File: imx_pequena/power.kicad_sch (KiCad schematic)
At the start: 25 parts

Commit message: Updated config
Updated config file and some pins
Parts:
- gave numbers to parts that had none: 25

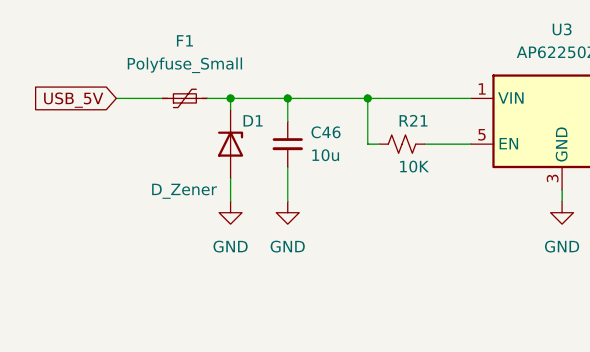
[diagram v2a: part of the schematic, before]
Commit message: Cleaned up NVCC pins
Added 3v3 connections + decoupling caps to NVcc pins
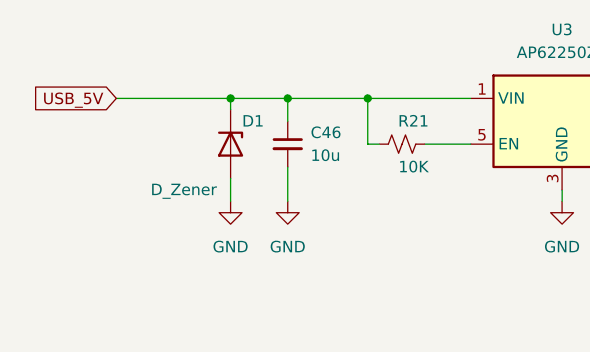
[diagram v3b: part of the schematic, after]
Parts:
- removed F1: Polyfuse_Small, symbol Device:Polyfuse_Small
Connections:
- net USB_5V: now also C46.1, D1.1 (K), R21.1, U3.1 (VIN)
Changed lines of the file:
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@@
-    (stroke (width 0) (type default) (color 0 0 0 0))
-  )
-  (wire (pts (xy 73.66 54.61) (xy 76.2 54.61))
     (stroke (width 0) (type default) (color 0 0 0 0))
   )
@@
     (stroke (width 0) (type default) (color 0 0 0 0))
   )
-  (wire (pts (xy 63.5 54.61) (xy 68.58 54.61))
+  (wire (pts (xy 63.5 54.61) (xy 76.2 54.61))
     (stroke (width 0) (type default) (color 0 0 0 0))
   )
@@
       (effects (font (size 1.27 1.27)) hide)
     )
-    (pin "1")
-    (pin "2")
-  )
-  (symbol (lib_id "Device:Polyfuse_Small") (at 71.12 54.61 90) (unit 1)
-    (in_bom yes) (on_board yes) (fields_autoplaced)
-    (property "Reference" "F1" (id 0) (at 71.12 48.26 90))
-    (property "Value" "Polyfuse_Small" (id 1) (at 71.12 50.8 90))
-    (property "Footprint" "" (id 2) (at 76.2 53.34 0)
-      (effects (font (size 1.27 1.27)) (justify left) hide)
-    )
-    (property "Datasheet" "~" (id 3) (at 71.12 54.61 0)
-      (effects (font (size 1.27 1.27)) hide)
-    )

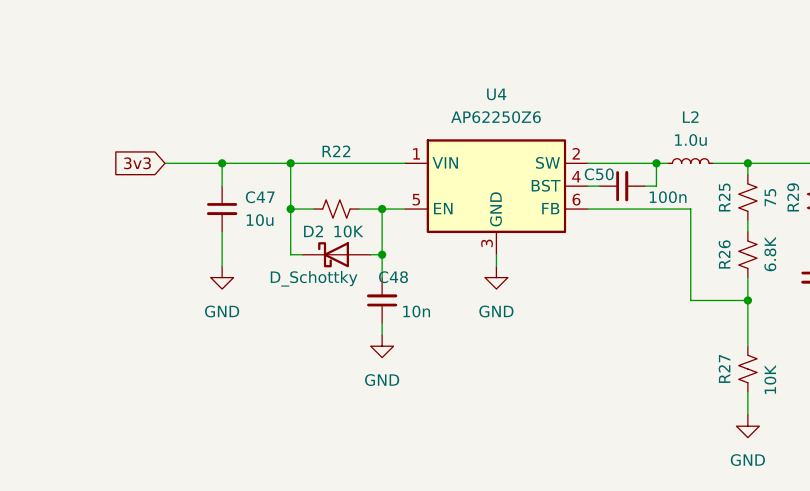
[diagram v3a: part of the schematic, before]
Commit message: Part Assignment
Assigned GPIOs and assigned footprints to most parts
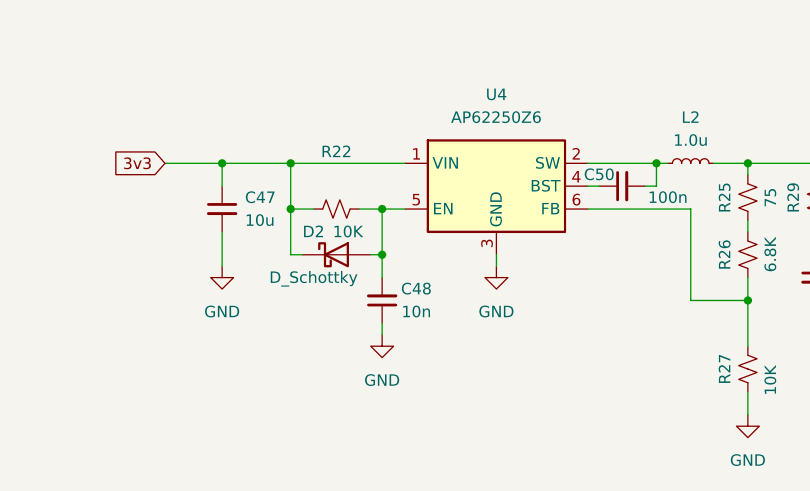
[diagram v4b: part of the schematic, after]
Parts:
- C46, C47, C48, C51, C52, C53, C54: footprint (none) -> Capacitor_SMD:C_0805_2012Metric
- C49, C50: footprint (none) -> Capacitor_SMD:C_0402_1005Metric
- D1, D2: footprint (none) -> Diode_SMD:D_SOD-123
- L1, L2: footprint (none) -> Inductor_SMD:L_Bourns_SRP5030T
- R21, R22, R23, R24, R25, R26, R27: footprint (none) -> Resistor_SMD:R_0402_1005Metric
- R28, R29: footprint (none) -> Resistor_SMD:R_0805_2012Metric
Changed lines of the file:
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@@
       (effects (font (size 1.27 1.27)) (justify left))
     )
-    (property "Footprint" "" (id 2) (at 76.2 59.69 0)
+    (property "Footprint" "Diode_SMD:D_SOD-123" (id 2) (at 76.2 59.69 0)
       (effects (font (size 1.27 1.27)) hide)
     )
@@
     (property "Reference" "L2" (id 0) (at 134.62 93.98 90))
     (property "Value" "1.0u" (id 1) (at 134.62 96.52 90))
-    (property "Footprint" "" (id 2) (at 134.62 99.06 0)
+    (property "Footprint" "Inductor_SMD:L_Bourns_SRP5030T" (id 2) (at 134.62 99.06 0)
       (effects (font (size 1.27 1.27)) hide)
     )
@@
     (property "Reference" "R25" (id 0) (at 138.43 102.87 90))
     (property "Value" "75" (id 1) (at 143.51 102.87 90))
-    (property "Footprint" "" (id 2) (at 140.97 102.87 0)
+    (property "Footprint" "Resistor_SMD:R_0402_1005Metric" (id 2) (at 140.97 102.87 0)
       (effects (font (size 1.27 1.27)) hide)
     )
@@
     (property "Reference" "C50" (id 0) (at 124.46 100.33 90))
     (property "Value" "100n" (id 1) (at 132.08 102.87 90))
-    (property "Footprint" "" (id 2) (at 127 101.6 0)
+    (property "Footprint" "Capacitor_SMD:C_0402_1005Metric" (id 2) (at 127 101.6 0)
       (effects (font (size 1.27 1.27)) hide)
     )
@@
     (property "Reference" "R24" (id 0) (at 138.43 68.58 90))
     (property "Value" "10K" (id 1) (at 143.51 69.85 90))
-    (property "Footprint" "" (id 2) (at 140.97 68.58 0)
+    (property "Footprint" "Resistor_SMD:R_0402_1005Metric" (id 2) (at 140.97 68.58 0)
       (effects (font (size 1.27 1.27)) hide)
     )
@@
     (property "Reference" "R29" (id 0) (at 146.05 102.87 90))
     (property "Value" "0.1" (id 1) (at 151.13 101.6 90))
-    (property "Footprint" "" (id 2) (at 148.59 102.87 0)
+    (property "Footprint" "Resistor_SMD:R_0805_2012Metric" (id 2) (at 148.59 102.87 0)
       (effects (font (size 1.27 1.27)) hide)
     )
@@
       (effects (font (size 1.27 1.27)) (justify left))
     )
-    (property "Footprint" "" (id 2) (at 156.21 111.76 0)
+    (property "Footprint" "Capacitor_SMD:C_0805_2012Metric" (id 2) (at 156.21 111.76 0)
       (effects (font (size 1.27 1.27)) hide)
     )
@@
       (effects (font (size 1.27 1.27)) (justify left))
     )
-    (property "Footprint" "" (id 2) (at 156.21 67.31 0)
+    (property "Footprint" "Capacitor_SMD:C_0805_2012Metric" (id 2) (at 156.21 67.31 0)
       (effects (font (size 1.27 1.27)) hide)
     )
@@
     (property "Reference" "R23" (id 0) (at 138.43 58.42 90))
     (property "Value" "31.6K" (id 1) (at 143.51 58.42 90))
-    (property "Footprint" "" (id 2) (at 140.97 58.42 0)
+    (property "Footprint" "Resistor_SMD:R_0402_1005Metric" (id 2) (at 140.97 58.42 0)
       (effects (font (size 1.27 1.27)) hide)
     )
@@
       (effects (font (size 1.27 1.27)) (justify left))
     )
-    (property "Footprint" "" (id 2) (at 148.59 111.76 0)
+    (property "Footprint" "Capacitor_SMD:C_0805_2012Metric" (id 2) (at 148.59 111.76 0)
       (effects (font (size 1.27 1.27)) hide)
     )
@@
     (property "Reference" "R21" (id 0) (at 96.52 57.15 90))
     (property "Value" "10K" (id 1) (at 96.52 62.23 90))
-    (property "Footprint" "" (id 2) (at 95.25 59.69 0)
+    (property "Footprint" "Resistor_SMD:R_0402_1005Metric" (id 2) (at 95.25 59.69 0)
       (effects (font (size 1.27 1.27)) hide)
     )
@@
     (property "Reference" "R28" (id 0) (at 146.05 58.42 90))
     (property "Value" "0.1" (id 1) (at 151.13 57.15 90))
-    (property "Footprint" "" (id 2) (at 148.59 58.42 0)
+    (property "Footprint" "Resistor_SMD:R_0805_2012Metric" (id 2) (at 148.59 58.42 0)
       (effects (font (size 1.27 1.27)) hide)
     )
@@
     (property "Reference" "R26" (id 0) (at 138.43 109.22 90))
     (property "Value" "6.8K" (id 1) (at 143.51 109.22 90))
-    (property "Footprint" "" (id 2) (at 140.97 109.22 0)
+    (property "Footprint" "Resistor_SMD:R_0402_1005Metric" (id 2) (at 140.97 109.22 0)
       (effects (font (size 1.27 1.27)) hide)
     )
@@
     (property "Reference" "L1" (id 0) (at 134.62 49.53 90))
     (property "Value" "2.2u" (id 1) (at 134.62 52.07 90))
-    (property "Footprint" "" (id 2) (at 134.62 54.61 0)
+    (property "Footprint" "Inductor_SMD:L_Bourns_SRP5030T" (id 2) (at 134.62 54.61 0)
       (effects (font (size 1.27 1.27)) hide)
     )
@@
       (effects (font (size 1.27 1.27)) (justify left))
     )
-    (property "Footprint" "" (id 2) (at 82.55 104.14 0)
+    (property "Footprint" "Capacitor_SMD:C_0805_2012Metric" (id 2) (at 82.55 104.14 0)
       (effects (font (size 1.27 1.27)) hide)
     )
@@
       (effects (font (size 1.27 1.27)) (justify left))
     )
-    (property "Footprint" "" (id 2) (at 82.55 59.69 0)
+    (property "Footprint" "Capacitor_SMD:C_0805_2012Metric" (id 2) (at 82.55 59.69 0)
       (effects (font (size 1.27 1.27)) hide)
     )
@@
   (symbol (lib_id "Device:C_Small") (at 100.33 114.3 180) (unit 1)
     (in_bom yes) (on_board yes)
-    (property "Reference" "C48" (id 0) (at 101.6 111.76 0))
+    (property "Reference" "C48" (id 0) (at 104.14 113.03 0))
     (property "Value" "10n" (id 1) (at 104.14 115.57 0))
-    (property "Footprint" "" (id 2) (at 100.33 114.3 0)
+    (property "Footprint" "Capacitor_SMD:C_0805_2012Metric" (id 2) (at 100.33 114.3 0)
       (effects (font (size 1.27 1.27)) hide)
     )
@@
     (property "Reference" "C49" (id 0) (at 124.46 55.88 90))
     (property "Value" "100n" (id 1) (at 132.08 58.42 90))
-    (property "Footprint" "" (id 2) (at 127 57.15 0)
+    (property "Footprint" "Capacitor_SMD:C_0402_1005Metric" (id 2) (at 127 57.15 0)
       (effects (font (size 1.27 1.27)) hide)
     )
@@
     (property "Reference" "D2" (id 0) (at 92.71 106.68 0))
     (property "Value" "D_Schottky" (id 1) (at 92.71 111.76 0))
-    (property "Footprint" "" (id 2) (at 95.25 109.22 0)
+    (property "Footprint" "Diode_SMD:D_SOD-123" (id 2) (at 95.25 109.22 0)
       (effects (font (size 1.27 1.27)) hide)
     )
@@
     (property "Reference" "R22" (id 0) (at 95.25 97.79 90))
     (property "Value" "10K" (id 1) (at 96.52 106.68 90))
-    (property "Footprint" "" (id 2) (at 95.25 104.14 0)
+    (property "Footprint" "Resistor_SMD:R_0402_1005Metric" (id 2) (at 95.25 104.14 0)
       (effects (font (size 1.27 1.27)) hide)
     )
@@
       (effects (font (size 1.27 1.27)) (justify left))
     )
-    (property "Footprint" "" (id 2) (at 148.59 67.31 0)
+    (property "Footprint" "Capacitor_SMD:C_0805_2012Metric" (id 2) (at 148.59 67.31 0)
       (effects (font (size 1.27 1.27)) hide)
     )
@@
     (property "Reference" "R27" (id 0) (at 138.43 121.92 90))
     (property "Value" "10K" (id 1) (at 143.51 123.19 90))
-    (property "Footprint" "" (id 2) (at 140.97 121.92 0)
-      (effects (font (size 1.27 1.27)) hide)
-    )
+    (property "Footprint" "Resistor_SMD:R_0402_1005Metric" (id 2) (at 140.97 121.92 0)
+      (effects (font (size 1.27 1.27)) hide)
+    )
